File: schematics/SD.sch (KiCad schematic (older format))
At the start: 5 parts, among them J12 SD_Switch, P1 SDCard

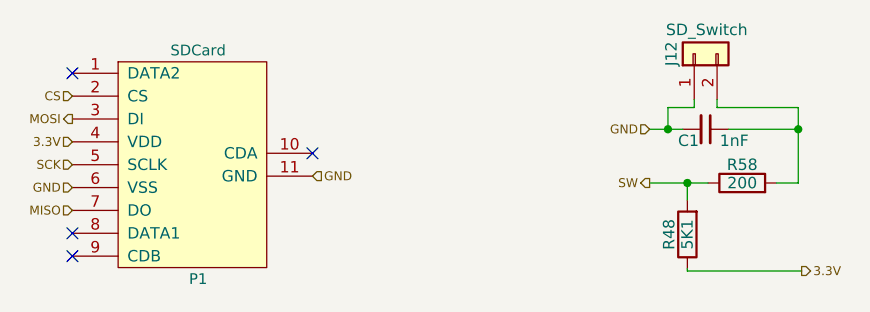
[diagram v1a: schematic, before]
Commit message: feat: external power circuit schematics
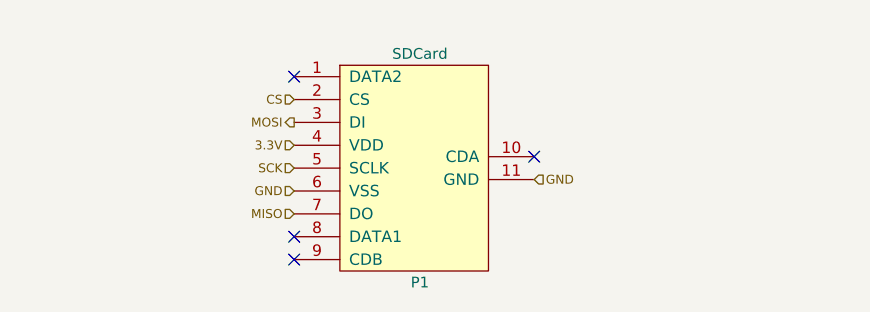
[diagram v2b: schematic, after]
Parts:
- removed C1: 1nF, Capacitors_SMD:C_0603, symbol Device:C_Small
- removed J12: SD_Switch, Button_Switch_SMD:SW_SPST_B3U-1000P, symbol PSLab-rescue:Conn_01x02
- removed R48: 5K1, Resistors_SMD:R_0603, symbol PSLab-rescue:R
- removed R58: 200, Resistors_SMD:R_0603, symbol PSLab-rescue:R
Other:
- moved on the sheet: P1
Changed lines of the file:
@@
 L PSLab:SDCard P1
 U 1 1 5C58B8EC
-P 4855 3555
-F 0 "P1" H 4855 2805 47  0000 C CNN
-F 1 "SDCard" H 4855 3805 47  0000 C CNN
-F 2 "Custom_Components:microSD_HC_Hirose_DM3AT-SF-PEJM5" H 4855 3555 60  0001 C CNN
-F 3 "" H 4855 3555 60  0001 C CNN
-	1    4855 3555
+P 5825 3570
+F 0 "P1" H 5825 2820 47  0000 C CNN
+F 1 "SDCard" H 5825 3820 47  0000 C CNN
+F 2 "Custom_Components:microSD_HC_Hirose_DM3AT-SF-PEJM5" H 5825 3570 60  0001 C CNN
+F 3 "" H 5825 3570 60  0001 C CNN
+	1    5825 3570
 	1    0    0    -1
 $EndComp
-NoConn ~ 4305 3405
-NoConn ~ 4305 4105
-NoConn ~ 4305 4205
-Text HLabel 5355 3855 2    39   Input ~ 0
+NoConn ~ 5275 3420
+NoConn ~ 5275 4120
+NoConn ~ 5275 4220
+Text HLabel 6325 3870 2    39   Input ~ 0
 GND
-Text HLabel 4305 3505 0    39   Input ~ 0
+Text HLabel 5275 3520 0    39   Input ~ 0
 CS
-Text HLabel 4305 3605 0    39   Output ~ 0
+Text HLabel 5275 3620 0    39   Output ~ 0
 MOSI
-Text HLabel 4305 3705 0    39   Input ~ 0
+Text HLabel 5275 3720 0    39   Input ~ 0
 3.3V
-Text HLabel 4305 3805 0    39   Input ~ 0
+Text HLabel 5275 3820 0    39   Input ~ 0
 SCK
-Text HLabel 4305 4005 0    39   Input ~ 0
+Text HLabel 5275 4020 0    39   Input ~ 0
 MISO
-NoConn ~ 5355 3755
-$Comp
-L PSLab-rescue:Conn_01x02 J?
-U 1 1 5C94297A
-P 7025 3320
-AR Path="/5C94297A" Ref="J?"  Part="1"
-AR Path="/5C58AFEF/5C94297A" Ref="J12"  Part="1"
-F 0 "J12" H 7025 3420 50  0000 C CNN
-F 1 "SD_Switch" V 7130 3265 50  0000 C CNN
-F 2 "Button_Switch_SMD:SW_SPST_B3U-1000P" H 7025 3320 50  0001 C CNN
-F 3 "" H 7025 3320 50  0001 C CNN
-	1    7025 3320
-	0    -1   -1   0
-$EndComp
-$Comp
-L PSLab-rescue:R R?
-U 1 1 5C942981
-P 6995 4110
-AR Path="/5C942981" Ref="R?"  Part="1"
-AR Path="/5C58AFEF/5C942981" Ref="R48"  Part="1"
-F 0 "R48" V 7075 4110 50  0000 C CNN
-F 1 "5K1" V 6995 4110 50  0000 C CNN
-F 2 "Resistors_SMD:R_0603" V 6925 4110 50  0001 C CNN
-F 3 "" H 6995 4110 50  0001 C CNN
-	1    6995 4110
-	-1   0    0    1
-$EndComp
-Wire Wire Line
-	6830 3885 6995 3885
-Wire Wire Line
-	6995 3885 6995 3960
-Connection ~ 6995 3885
-Wire Wire Line
-	6995 4270 6995 4260
-Wire Wire Line
-	6995 3885 7085 3885
-$Comp
-L PSLab-rescue:R R?
-U 1 1 5C942995
-P 7235 3885
-AR Path="/5C942995" Ref="R?"  Part="1"
-AR Path="/5C58AFEF/5C942995" Ref="R58"  Part="1"
-F 0 "R58" V 7315 3885 50  0000 C CNN
-F 1 "200" V 7235 3885 50  0000 C CNN
-F 2 "Resistors_SMD:R_0603" V 7165 3885 50  0001 C CNN
-F 3 "" H 7235 3885 50  0001 C CNN
-	1    7235 3885
-	0    -1   -1   0
-$EndComp
-Wire Wire Line
-	7480 3885 7385 3885
-$Comp
-L Device:C_Small C?
-U 1 1 5C94299D
-P 7075 3650
-AR Path="/5C94299D" Ref="C?"  Part="1"
-AR Path="/5C58AFEF/5C94299D" Ref="C1"  Part="1"
-F 0 "C1" V 7125 3575 50  0000 C CNN
-F 1 "1nF" V 7125 3775 50  0000 C CNN
-F 2 "Capacitors_SMD:C_0603" H 7075 3650 50  0001 C CNN
-F 3 "~" H 7075 3650 50  0001 C CNN
-	1    7075 3650
-	0    1    1    0
-$EndComp
-Wire Wire Line
-	6975 3650 6910 3650
-Wire Wire Line
-	7025 3520 7025 3555
-Wire Wire Line
-	7025 3555 6910 3555
-Wire Wire Line
-	6910 3555 6910 3650
-Connection ~ 6910 3650
-Wire Wire Line
-	6910 3650 6830 3650
-Wire Wire Line
-	7175 3650 7480 3650
-Wire Wire Line
-	7480 3650 7480 3885
-Wire Wire Line
-	7125 3520 7125 3555
-Wire Wire Line
-	7125 3555 7480 3555
-Wire Wire Line
-	7480 3555 7480 3650
-Connection ~ 7480 3650
-Wire Wire Line
-	7495 4270 6995 4270
-Text HLabel 7495 4270 2    39   Output ~ 0
-3.3V
-Text HLabel 6830 3885 0    39   Output ~ 0
-SW
-Text HLabel 6830 3650 0    39   Input ~ 0
-GND
-Text HLabel 4305 3905 0    39   Input ~ 0
+NoConn ~ 6325 3770
+Text HLabel 5275 3920 0    39   Input ~ 0
 GND
 $EndSCHEMATC

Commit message: feat: bom generator and updated project to support bom generator
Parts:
- P1: footprint Custom_Components:microSD_HC_Hirose_DM3AT-SF-PEJM5 -> PSLab:microSD_HC_Hirose_DM3AT-SF-PEJM5; Description (none) -> 8P R/A SMT MICRO SD PUSH-PUSH; Mfr No. (none) -> DM3AT-SF-PEJM5(11); PartNumber (none) -> DM3AT-SF-PEJM5(11); Price (none) -> 2.45
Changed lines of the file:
@@
 F 0 "P1" H 5825 2820 47  0000 C CNN
 F 1 "SDCard" H 5825 3820 47  0000 C CNN
-F 2 "Custom_Components:microSD_HC_Hirose_DM3AT-SF-PEJM5" H 5825 3570 60  0001 C CNN
-F 3 "" H 5825 3570 60  0001 C CNN
+F 2 "PSLab:microSD_HC_Hirose_DM3AT-SF-PEJM5" H 5825 3570 60  0001 C CNN
+F 3 "https://eu.mouser.com/datasheet/2/185/DM3_catalog-939223.pdf" H 5825 3570 60  0001 C CNN
+F 4 "8P R/A SMT MICRO SD PUSH-PUSH" H 5825 3570 50  0001 C CNN "Description"
+F 5 "DM3AT-SF-PEJM5(11)" H 5825 3570 50  0001 C CNN "Mfr No."
+F 6 "DM3AT-SF-PEJM5(11)" H 5825 3570 50  0001 C CNN "PartNumber"
+F 7 "2.45" H 5825 3570 50  0001 C CNN "Price"
 	1    5825 3570
 	1    0    0    -1
